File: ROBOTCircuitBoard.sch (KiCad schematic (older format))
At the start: 18 parts, among them J1 DB15_HighDensity_MountingHoles, J2 DB15_HighDensity_MountingHoles, P1 CONN_01X03, P13 CONN_01X04, P15 CONN_01X04, P2 CONN_01X04, P24 CONN_01X04, P3 CONN_01X04, P4 CONN_01X04, P5 CONN_01X05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

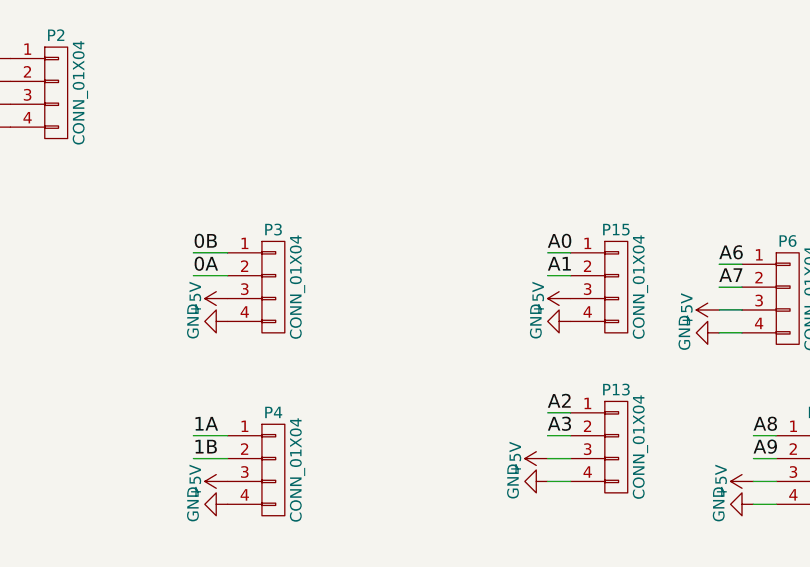
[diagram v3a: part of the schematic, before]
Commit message: Fixed silkscreen and began more organized board, not used.
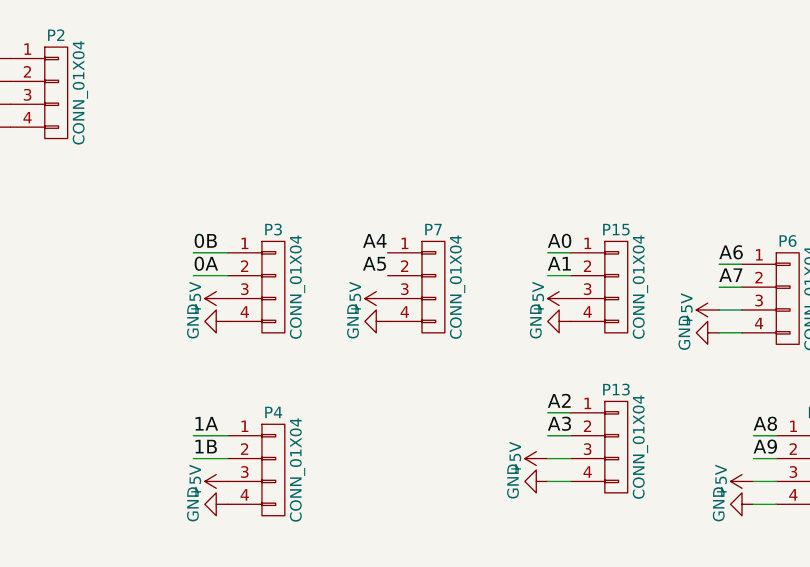
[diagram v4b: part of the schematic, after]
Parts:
- added P7: CONN_01X04, Socket_Strips:Socket_Strip_Straight_1x04_Pitch2.54mm, symbol CONN_01X04
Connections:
- net +5V: now also P7.3 (P3)
- net A4: now also P7.1 (P1)
- net A5: now also P7.2 (P2)
- net GND: now also P7.4 (P4)
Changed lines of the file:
@@
 Text Label 3950 6200 0    60   ~ 0
 A9
+$Comp
+L CONN_01X04 P7
+U 1 1 58D31748
+P 7500 5100
+F 0 "P7" H 7500 5350 50  0000 C CNN
+F 1 "CONN_01X04" V 7600 5100 50  0000 C CNN
+F 2 "Socket_Strips:Socket_Strip_Straight_1x04_Pitch2.54mm" H 7500 5100 50  0001 C CNN
+F 3 "" H 7500 5100 50  0000 C CNN
+	1    7500 5100
+	1    0    0    -1
+$EndComp
+$Comp
+L GND #PWR047
+U 1 1 58D317F9
+P 7300 5250
+F 0 "#PWR047" H 7300 5000 50  0001 C CNN
+F 1 "GND" H 7300 5100 50  0000 C CNN
+F 2 "" H 7300 5250 50  0000 C CNN
+F 3 "" H 7300 5250 50  0000 C CNN
+	1    7300 5250
+	0    1    1    0
+$EndComp
+$Comp
+L +5V #PWR048
+U 1 1 58D3182C
+P 7300 5150
+F 0 "#PWR048" H 7300 5000 50  0001 C CNN
+F 1 "+5V" H 7300 5290 50  0000 C CNN
+F 2 "" H 7300 5150 50  0000 C CNN
+F 3 "" H 7300 5150 50  0000 C CNN
+	1    7300 5150
+	0    -1   -1   0
+$EndComp
+Text Label 7300 4950 2    60   ~ 0
+A4
+Text Label 7300 5050 2    60   ~ 0
+A5
 $EndSCHEMATC
